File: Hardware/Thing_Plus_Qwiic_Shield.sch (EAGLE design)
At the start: 16 parts, among them J1 QWIIC_RIGHT_ANGLE, J2 QWIIC_RIGHT_ANGLE, J3 Vertical Qwiic Connector, J4 Vertical Qwiic Connector, U1 THING_PLUS

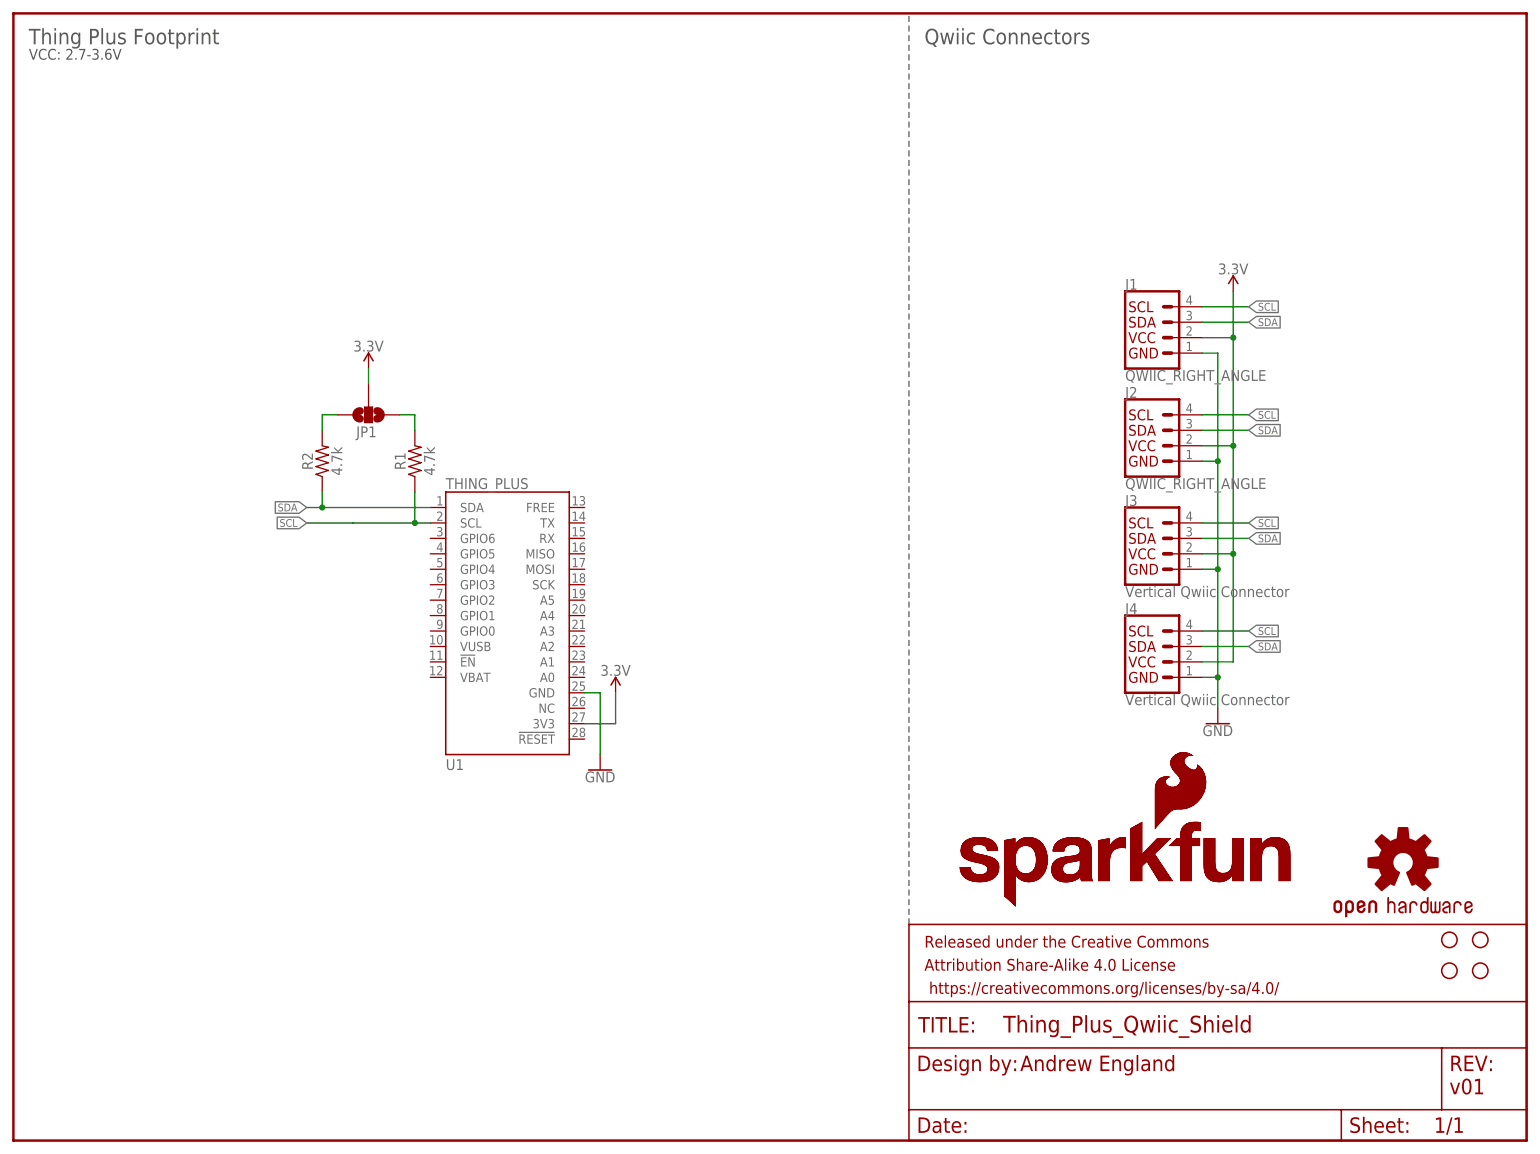
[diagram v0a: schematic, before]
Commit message: panelizing and uploading gerbers
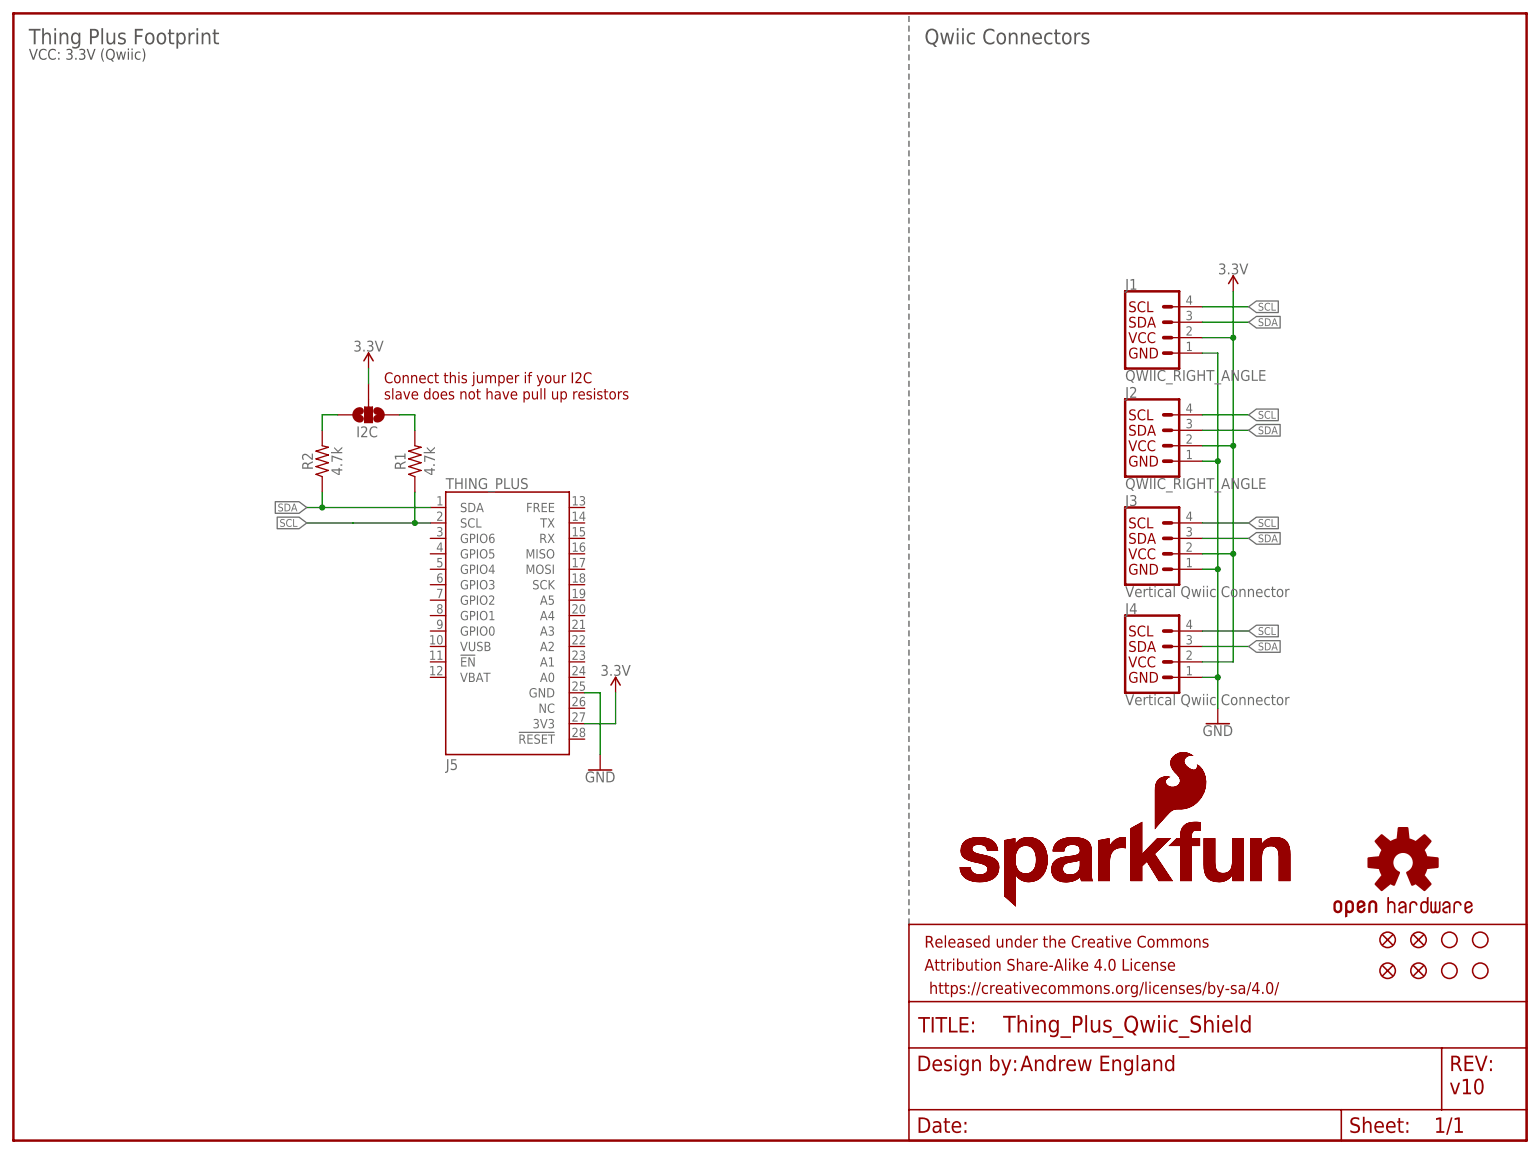
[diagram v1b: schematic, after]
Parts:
- added FD1, FD2, FD3, FD4: FIDUCIAL1X2, SparkFun-Aesthetics:FIDUCIAL1X2
- renumbered JP1 to I2C, U1 to J5
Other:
- note added: "Connect this jumper if your I2C slave does not have pull up resistors"
- note added: "VCC: 3.3V (Qwiic)"
- note added: "v10"
- note removed: "VCC: 2.7-3.6V"
- note removed: "v01"
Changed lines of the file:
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@@
 <parts>
 <part name="FRAME1" library="SparkFun-Aesthetics" deviceset="FRAME-LETTER" device=""/>
-<part name="U1" library="SparkFun-Boards" deviceset="THING_PLUS" device=""/>
+<part name="J5" library="SparkFun-Boards" deviceset="THING_PLUS" device=""/>
 <part name="J1" library="SparkFun-Connectors" deviceset="QWIIC_CONNECTOR" device="JS-1MM" value="QWIIC_RIGHT_ANGLE"/>
 <part name="J2" library="SparkFun-Connectors" deviceset="QWIIC_CONNECTOR" device="JS-1MM" value="QWIIC_RIGHT_ANGLE"/>
@@
 <part name="R1" library="SparkFun-Resistors" deviceset="4.7KOHM" device="-0603-1/10W-1%" value="4.7k"/>
 <part name="R2" library="SparkFun-Resistors" deviceset="4.7KOHM" device="-0603-1/10W-1%" value="4.7k"/>
-<part name="JP1" library="SparkFun-Jumpers" deviceset="JUMPER-SMT_3_NO" device="_NO-SILK" package3d_urn="urn:adsk.eagle:package:39284/1"/>
+<part name="I2C" library="SparkFun-Jumpers" deviceset="JUMPER-SMT_3_NO" device="_NO-SILK" package3d_urn="urn:adsk.eagle:package:39284/1"/>
 <part name="SUPPLY2" library="SparkFun-PowerSymbols" deviceset="3.3V" device=""/>
 <part name="SUPPLY3" library="SparkFun-PowerSymbols" deviceset="3.3V" device=""/>
@@
 <part name="LOGO2" library="SparkFun-Aesthetics" deviceset="SFE_LOGO_NAME_FLAME" device=".2_INCH" value="SFE_LOGO_NAME_FLAME.2_INCH"/>
 <part name="LOGO3" library="SparkFun-Aesthetics" deviceset="OSHW-LOGO" device="S"/>
+<part name="FD1" library="SparkFun-Aesthetics" deviceset="FIDUCIAL" device="1X2"/>
+<part name="FD2" library="SparkFun-Aesthetics" deviceset="FIDUCIAL" device="1X2"/>
+<part name="FD3" library="SparkFun-Aesthetics" deviceset="FIDUCIAL" device="1X2"/>
+<part name="FD4" library="SparkFun-Aesthetics" deviceset="FIDUCIAL" device="1X2"/>
 </parts>
 <sheets>
@@
 <plain>
 <text x="165.608" y="11.43" size="2.54" layer="94" font="vector">Andrew England</text>
-<text x="236.22" y="7.62" size="2.54" layer="94" font="vector">v01</text>
+<text x="236.22" y="7.62" size="2.54" layer="94" font="vector">v10</text>
 <wire x1="147.32" y1="35.56" x2="147.32" y2="185.42" width="0.2032" layer="97" style="longdash"/>
 <text x="2.54" y="180.34" size="2.54" layer="97" font="vector">Thing Plus Footprint</text>
 <text x="149.86" y="180.34" size="2.54" layer="97" font="vector">Qwiic Connectors</text>
-<text x="2.54" y="177.8" size="1.778" layer="97" font="vector">VCC: 2.7-3.6V</text>
+<text x="2.54" y="177.8" size="1.778" layer="97" font="vector">VCC: 3.3V (Qwiic)</text>
+<text x="60.96" y="121.92" size="1.778" layer="94" font="vector">Connect this jumper if your I2C
+slave does not have pull up resistors</text>
 </plain>
 <instances>
 <instance part="FRAME1" gate="G$1" x="0" y="0"/>
 <instance part="FRAME1" gate="V" x="147.32" y="0"/>
-<instance part="U1" gate="G$1" x="81.28" y="93.98"/>
+<instance part="J5" gate="G$1" x="81.28" y="93.98"/>
 <instance part="J1" gate="G$1" x="187.96" y="132.08"/>
 <instance part="J2" gate="G$1" x="187.96" y="114.3"/>
@@
 <instance part="R1" gate="G$1" x="66.04" y="111.76" rot="R90"/>
 <instance part="R2" gate="G$1" x="50.8" y="111.76" rot="R90"/>
-<instance part="JP1" gate="G$1" x="58.42" y="119.38" smashed="yes" rot="R270">
+<instance part="I2C" gate="G$1" x="58.42" y="119.38" smashed="yes" rot="R270">
 <attribute name="NAME" x="56.388" y="115.697" size="1.778" layer="95" font="vector"/>
 </instance>
@@
 <instance part="LOGO2" gate="G$1" x="154.94" y="38.1"/>
 <instance part="LOGO3" gate="G$1" x="228.6" y="45.72"/>
+<instance part="FD1" gate="G$1" x="231.14" y="33.02"/>
+<instance part="FD2" gate="G$1" x="226.06" y="33.02"/>
+<instance part="FD3" gate="G$1" x="226.06" y="27.94"/>
+<instance part="FD4" gate="G$1" x="231.14" y="27.94"/>
 </instances>
 <busses>
@@
 </segment>
 <segment>
-<pinref part="U1" gate="G$1" pin="GND"/>
+<pinref part="J5" gate="G$1" pin="GND"/>
 <pinref part="GND2" gate="1" pin="GND"/>
 <wire x1="93.98" y1="73.66" x2="96.52" y2="73.66" width="0.1524" layer="91"/>
@@
 </segment>
 <segment>
-<pinref part="JP1" gate="G$1" pin="2"/>
+<pinref part="I2C" gate="G$1" pin="2"/>
 <pinref part="SUPPLY2" gate="G$1" pin="3.3V"/>
 <wire x1="58.42" y1="127" x2="58.42" y2="124.46" width="0.1524" layer="91"/>
 </segment>
 <segment>
-<pinref part="U1" gate="G$1" pin="3V3"/>
+<pinref part="J5" gate="G$1" pin="3V3"/>
 <wire x1="93.98" y1="68.58" x2="99.06" y2="68.58" width="0.1524" layer="91"/>
 <pinref part="SUPPLY3" gate="G$1" pin="3.3V"/>
@@
 </segment>
 <segment>
-<pinref part="U1" gate="G$1" pin="SDA"/>
+<pinref part="J5" gate="G$1" pin="SDA"/>
 <wire x1="68.58" y1="104.14" x2="50.8" y2="104.14" width="0.1524" layer="91"/>
 <pinref part="R2" gate="G$1" pin="1"/>
@@
 </segment>
 <segment>
-<pinref part="U1" gate="G$1" pin="SCL"/>
+<pinref part="J5" gate="G$1" pin="SCL"/>
 <wire x1="68.58" y1="101.6" x2="66.04" y2="101.6" width="0.1524" layer="91"/>
 <pinref part="R1" gate="G$1" pin="1"/>
@@
 <pinref part="R2" gate="G$1" pin="2"/>
 <wire x1="50.8" y1="116.84" x2="50.8" y2="119.38" width="0.1524" layer="91"/>
-<pinref part="JP1" gate="G$1" pin="3"/>
+<pinref part="I2C" gate="G$1" pin="3"/>
 <wire x1="50.8" y1="119.38" x2="53.34" y2="119.38" width="0.1524" layer="91"/>
 </segment>
@@
 <net name="N$4" class="0">
 <segment>
-<pinref part="JP1" gate="G$1" pin="1"/>
+<pinref part="I2C" gate="G$1" pin="1"/>
 <pinref part="R1" gate="G$1" pin="2"/>
 <wire x1="63.5" y1="119.38" x2="66.04" y2="119.38" width="0.1524" layer="91"/>
@@
 </drawing>
 <compatibility>
+<note version="6.3" minversion="6.2.2" severity="warning">
+Since Version 6.2.2 text objects can contain more than one line,
+which will not be processed correctly with this version.
+</note>
 <note version="8.3" severity="warning">
 Since Version 8.3, EAGLE supports URNs for individual library
